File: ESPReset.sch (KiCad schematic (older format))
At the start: 3 parts, among them Q2 MMDT3904

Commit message: Add JCLPCB/LCSC part numbers
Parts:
- Q2: LCSC (none) -> C155305
- R21, R22: LCSC (none) -> C17414
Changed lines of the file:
@@
 EESchema Schematic File Version 4
+LIBS:ULPSoilMonitor-cache
 EELAYER 30 0
 EELAYER END
@@
 F 2 "Package_TO_SOT_SMD:SOT-363_SC-70-6" H 2300 1100 50  0001 C CNN
 F 3 "http://www.diodes.com/_files/datasheets/ds30088.pdf" H 2100 1000 50  0001 C CNN
+F 4 "C155305" H 2100 1000 50  0001 C CNN "LCSC"
 	1    2100 1000
 	1    0    0    -1
@@
 F 2 "Package_TO_SOT_SMD:SOT-363_SC-70-6" H 2300 1750 50  0001 C CNN
 F 3 "http://www.diodes.com/_files/datasheets/ds30088.pdf" H 2100 1650 50  0001 C CNN
+F 4 "C155305" H 2100 1650 50  0001 C CNN "LCSC"
 	2    2100 1650
 	1    0    0    -1
@@
 F 2 "Resistor_SMD:R_0805_2012Metric" V 1480 1000 50  0001 C CNN
 F 3 "~" H 1550 1000 50  0001 C CNN
+F 4 "C17414" H 1550 1000 50  0001 C CNN "LCSC"
 	1    1550 1000
 	0    1    1    0
@@
 F 2 "Resistor_SMD:R_0805_2012Metric" V 1480 1650 50  0001 C CNN
 F 3 "~" H 1550 1650 50  0001 C CNN
+F 4 "C17414" H 1550 1650 50  0001 C CNN "LCSC"
 	1    1550 1650
 	0    1    1    0

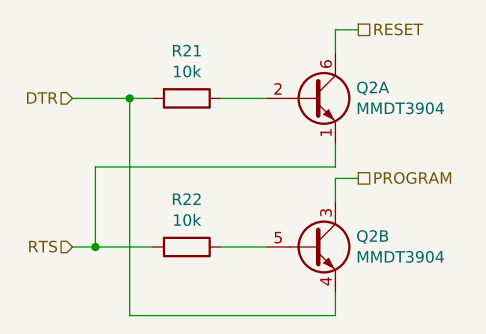
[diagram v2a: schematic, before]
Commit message: Set USB-serial DNP
Disable USB-serial
Add switches for LiFePo charger PROG setting
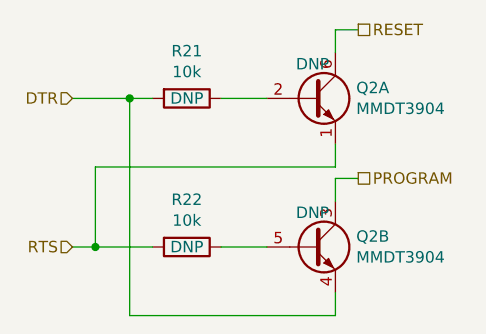
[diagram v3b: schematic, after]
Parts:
- Q2, R21, R22: DNP (none) -> DNP
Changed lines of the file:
@@
 $EndDescr
-$Comp
-L Transistor_BJT:MMDT3904 Q?
-U 1 1 5F05912F
-P 2100 1000
-AR Path="/5F05912F" Ref="Q?"  Part="1"
-AR Path="/5F0560DE/5F05912F" Ref="Q2"  Part="1"
-F 0 "Q2" H 2291 1046 50  0000 L CNN
-F 1 "MMDT3904" H 2291 955 50  0000 L CNN
-F 2 "Package_TO_SOT_SMD:SOT-363_SC-70-6" H 2300 1100 50  0001 C CNN
-F 3 "http://www.diodes.com/_files/datasheets/ds30088.pdf" H 2100 1000 50  0001 C CNN
-F 4 "C155305" H 2100 1000 50  0001 C CNN "LCSC"
-	1    2100 1000
-	1    0    0    -1
-$EndComp
-$Comp
-L Transistor_BJT:MMDT3904 Q?
-U 2 1 5F059135
-P 2100 1650
-AR Path="/5F059135" Ref="Q?"  Part="2"
-AR Path="/5F0560DE/5F059135" Ref="Q2"  Part="2"
-F 0 "Q2" H 2291 1696 50  0000 L CNN
-F 1 "MMDT3904" H 2291 1605 50  0000 L CNN
-F 2 "Package_TO_SOT_SMD:SOT-363_SC-70-6" H 2300 1750 50  0001 C CNN
-F 3 "http://www.diodes.com/_files/datasheets/ds30088.pdf" H 2100 1650 50  0001 C CNN
-F 4 "C155305" H 2100 1650 50  0001 C CNN "LCSC"
-	2    2100 1650
-	1    0    0    -1
-$EndComp
 $Comp
 L Device:R R?
@@
 F 3 "~" H 1550 1000 50  0001 C CNN
 F 4 "C17414" H 1550 1000 50  0001 C CNN "LCSC"
+F 5 "DNP" V 1550 1000 50  0000 C CNN "DNP"
 	1    1550 1000
 	0    1    1    0
@@
 F 3 "~" H 1550 1650 50  0001 C CNN
 F 4 "C17414" H 1550 1650 50  0001 C CNN "LCSC"
+F 5 "DNP" V 1550 1650 50  0000 C CNN "DNP"
 	1    1550 1650
 	0    1    1    0
@@
 Text HLabel 1050 1650 0    50   Input ~ 0
 RTS
+$Comp
+L Transistor_BJT:MMDT3904 Q?
+U 2 1 5F059135
+P 2100 1650
+AR Path="/5F059135" Ref="Q?"  Part="2"
+AR Path="/5F0560DE/5F059135" Ref="Q2"  Part="2"
+F 0 "Q2" H 2291 1696 50  0000 L CNN
+F 1 "MMDT3904" H 2291 1605 50  0000 L CNN
+F 2 "Package_TO_SOT_SMD:SOT-363_SC-70-6" H 2300 1750 50  0001 C CNN
+F 3 "http://www.diodes.com/_files/datasheets/ds30088.pdf" H 2100 1650 50  0001 C CNN
+F 4 "C155305" H 2100 1650 50  0001 C CNN "LCSC"
+F 5 "DNP" H 2100 1800 50  0000 C CNN "DNP"
+	2    2100 1650
+	1    0    0    -1
+$EndComp
+$Comp
+L Transistor_BJT:MMDT3904 Q?
+U 1 1 5F05912F
+P 2100 1000
+AR Path="/5F05912F" Ref="Q?"  Part="1"
+AR Path="/5F0560DE/5F05912F" Ref="Q2"  Part="1"
+F 0 "Q2" H 2291 1046 50  0000 L CNN
+F 1 "MMDT3904" H 2291 955 50  0000 L CNN
+F 2 "Package_TO_SOT_SMD:SOT-363_SC-70-6" H 2300 1100 50  0001 C CNN
+F 3 "http://www.diodes.com/_files/datasheets/ds30088.pdf" H 2100 1000 50  0001 C CNN
+F 4 "C155305" H 2100 1000 50  0001 C CNN "LCSC"
+F 5 "DNP" H 2100 1150 50  0000 C CNN "DNP"
+	1    2100 1000
+	1    0    0    -1
+$EndComp
 $EndSCHEMATC
